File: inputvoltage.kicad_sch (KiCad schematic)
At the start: 2 parts

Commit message: Temp Update
Added comments, Op Amp, changed tags, added some wiring, prepared for finalization of Schematic.
(Still missing some values)
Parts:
- R5: value 75 kOhm -> 125 kOhm
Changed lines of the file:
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@@
 			)
 		)
-		(property "Value" "75 kOhm"
+		(property "Value" "125 kOhm"
 			(at 142.24 81.2799 0)
 			(effects

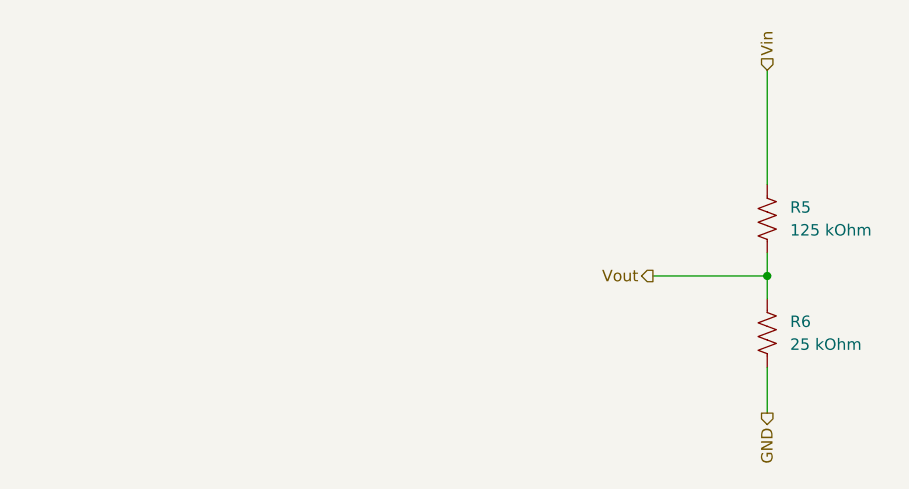
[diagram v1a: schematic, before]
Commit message: Schematic Complete
Completed the wiring of the circuit.

(Missing some labels and footprints)
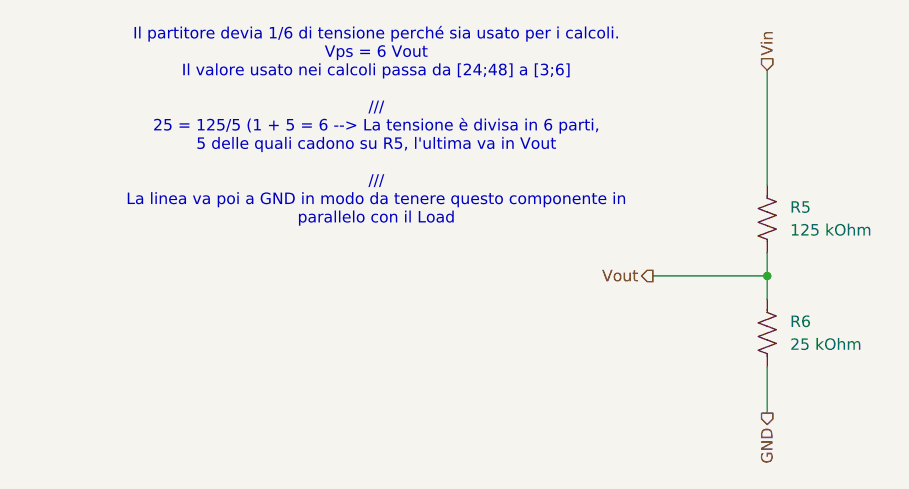
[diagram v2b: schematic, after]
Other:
- note added: "Il partitore devia 1/6 di tensione perché sia usato per i calcoli. Vps = 6 Vout Il valore usato nei calcoli passa da [24;48] a [3;6] /// 25 = 125/5 (1 + 5 = 6 --> La tensione è divisa in 6 parti, 5 delle quali cadono su R5, l'ultima va in Vout /// La linea va poi a GND in modo da tenere questo componente in parallelo con il Load"
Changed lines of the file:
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@@
 	(generator_version "9.0")
 	(paper "A4")
+	(text "Il partitore devia 1/6 di tensione perché sia usato per i calcoli.\nVps = 6 Vout\nIl valore usato nei calcoli passa da [24;48] a [3;6]\n\n///\n25 = 125/5 (1 + 5 = 6 --> La tensione è divisa in 6 parti,\n5 delle quali cadono su R5, l'ultima va in Vout\n\n///\nLa linea va poi a GND in modo da tenere questo componente in \nparallelo con il Load"
+		(exclude_from_sim no)
+		(at 96.266 69.85 0)
+		(effects
+			(font
+				(size 1.27 1.27)
+			)
+		)
+	)
 	(junction
 		(at 139.7 86.36)

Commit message: Finished (?)
Assigned al values, footprints and generated traces.
Generated DRL files.
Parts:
- R5, R6: footprint (none) -> Resistor_SMD:R_0805_2012Metric
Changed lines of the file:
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@@
 			)
 		)
-		(property "Footprint" ""
+		(property "Footprint" "Resistor_SMD:R_0805_2012Metric"
 			(at 140.716 80.264 90)
 			(effects
@@
 			)
 		)
-		(property "Footprint" ""
+		(property "Footprint" "Resistor_SMD:R_0805_2012Metric"
 			(at 140.716 92.964 90)
 			(effects
